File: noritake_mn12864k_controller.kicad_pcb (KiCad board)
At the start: 4 copper layers, 85 x 46.5 mm, 150 parts, among them J1 Conn_01x11, J2 USB_C_Receptacle_USB2.0, J3 TagConnect_TC2030_SWD, J4 Conn_01x18, Q1 AO3400A, Q10 2N7002, Q11 LBSS84LT1G, Q12 2N7002, Q13 TO-252, Q14 CJT04N15, Q15 2N7002, Q16 LBSS84LT1G, Q17 2N7002, Q18 S9015, Q2 AO3400A, Q3 S9015, Q4 AO3401A, Q5 AO3401A, Q6 S9015, Q7 2N7002, Q8 LBSS84LT1G, Q9 2N7002, T1 Wuerth 760390013, T2 Wuerth 760390013, T3 Wuerth 760390013, U1 SN74AVC8T245PW, U10 SRV05-4, U11 SRV05-4, U12 SRV05-4, U2 74HC14, U3 CD4051B, U4 MN12864K, U5 STM32F730R8T6, U6 NE555D, U7 74HC08, U8 SRV05-4, U9 XC6206PxxxMR

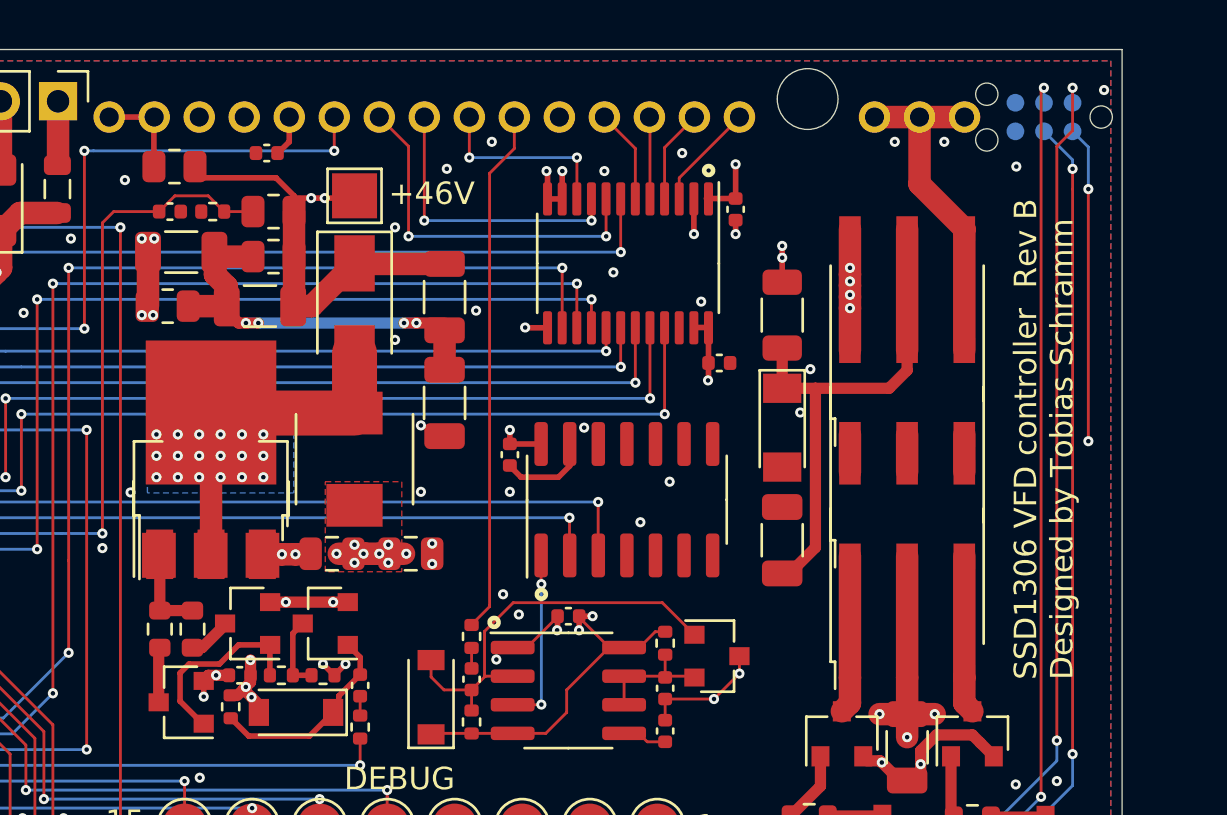
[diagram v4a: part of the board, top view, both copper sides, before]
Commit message: Add more VFD VDD2 bulk capacitance
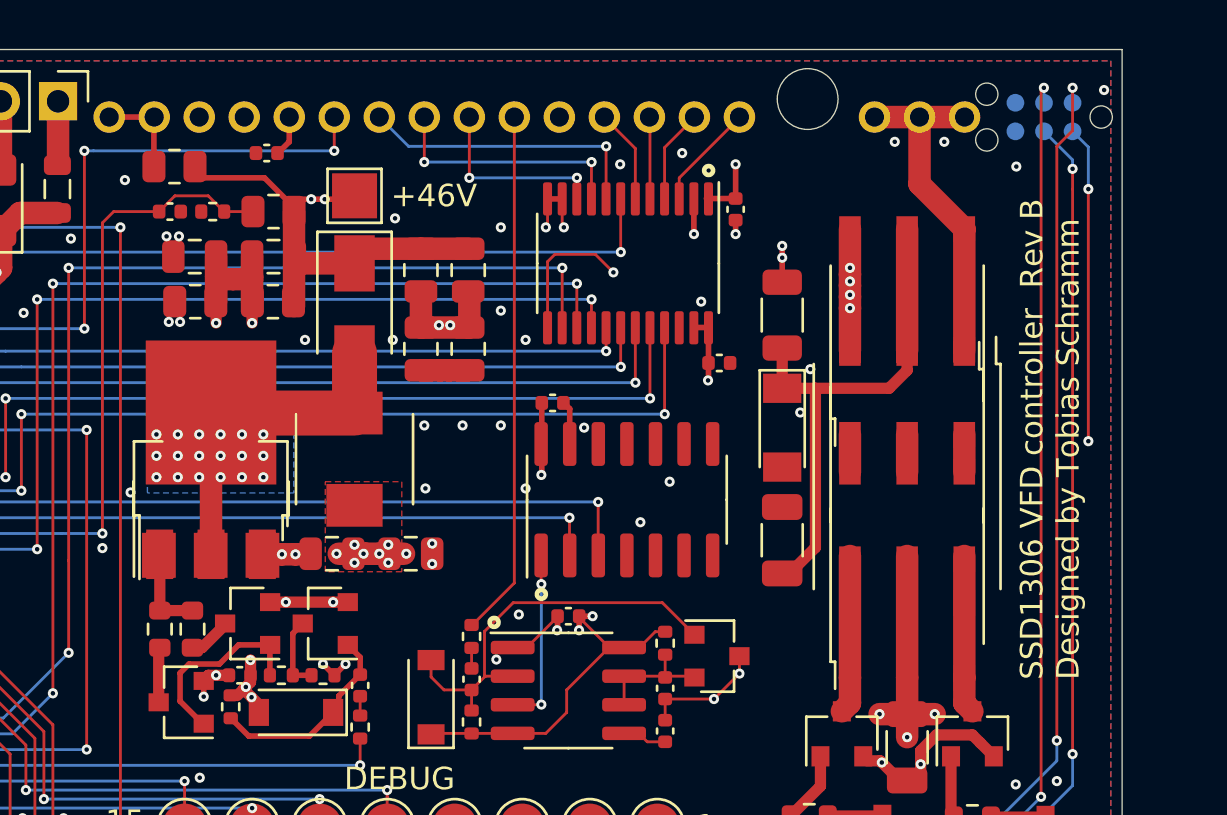
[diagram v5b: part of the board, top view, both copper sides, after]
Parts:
- added C40: 10uF, Capacitor_SMD:C_0805_2012Metric, F.Cu at (147.3, 104.7)
- added C41: 10uF, Capacitor_SMD:C_0805_2012Metric, F.Cu at (153.8, 108.8)
- added T4: Wuerth 760390013, Transformer_Würth:Transformer_Würth_12.60x8.30_6P, F.Cu at (175.4, 114.5)
- C30, C35, C38, C39: footprint Capacitor_SMD:C_1206_3216Metric -> Capacitor_SMD:C_0805_2012Metric
- moved C39 12.9 mm to (143.8, 104.7), turned to 180 degrees
- moved C35 12.8 mm to (155.9, 105.3), turned to 270 degrees
- moved C30 9.44 mm to (155.9, 108.8), turned to 270 degrees
- moved C27 2.98 mm to (159.7, 111.2), turned to 180 degrees
- moved R30 2.00 mm to (147.3, 106.7)
- moved C38 1.59 mm to (153.8, 105.3)
- moved R31 1.24 mm to (143.8, 106.7)
- turned T1 to 270 degrees
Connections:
- C30 pad 1: +48V -> Net-(C30-Pad1)
- C30 pad 2: Net-(C30-Pad2) -> GND
- C35 pad 1: Net-(C30-Pad2) -> +48V
- C35 pad 2: GND -> Net-(C30-Pad1)
- C38 pad 2: Net-(C30-Pad2) -> Net-(C30-Pad1)
- C39 pad 1: Net-(C30-Pad2) -> Net-(C30-Pad1)
- R30 pad 2: Net-(C30-Pad2) -> Net-(C30-Pad1)
- R31 pad 1: Net-(C30-Pad2) -> Net-(C30-Pad1)
- T1 pad 1: Net-(Q2-Pad3) -> Net-(T1-Pad1)
- T1 pad 2: +5V -> Net-(C8-Pad1)
- T1 pad 3: Net-(Q1-Pad3) -> Net-(T1-Pad3)
- T1 pad 4: Net-(T1-Pad4) -> Net-(Q2-Pad3)
- T1 pad 5: Net-(C8-Pad1) -> +5V
- T1 pad 6: Net-(T1-Pad6) -> Net-(Q1-Pad3)
- T3 pad 4: Net-(T1-Pad4) -> Net-(T1-Pad1)
- T3 pad 6: Net-(T1-Pad6) -> Net-(T1-Pad3)
- U4 pad 1: Net-(T1-Pad4) -> Net-(T1-Pad1)
- U4 pad 2: Net-(T1-Pad4) -> Net-(T1-Pad1)
- U4 pad 3: Net-(T1-Pad4) -> Net-(T1-Pad1)
- U4 pad 35: Net-(T1-Pad6) -> Net-(T1-Pad3)
- U4 pad 36: Net-(T1-Pad6) -> Net-(T1-Pad3)
- U4 pad 37: Net-(T1-Pad6) -> Net-(T1-Pad3)
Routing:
- net Net-(T1-Pad6): track 83.7 -> 0.00 mm, vias 4 -> 0
- net Net-(T1-Pad3): track 0.00 -> 83.7 mm, vias 0 -> 4
- net Net-(C30-Pad1): track 0.00 -> 23.5 mm, vias 0 -> 4
- net Net-(C30-Pad2): track 18.6 -> 0.00 mm, vias 4 -> 0
- net Net-(T1-Pad4): track 15.2 -> 0.00 mm
- net Net-(T1-Pad1): track 0.00 -> 15.2 mm
- net Net-(U1-Pad8): track 16.3 -> 13.0 mm, vias 2 -> 1
- net GND: track 88.8 -> 91.8 mm, vias 146 -> 147
- net Net-(U1-Pad9): track 13.0 -> 11.1 mm
- net +5V: track 76.3 -> 77.5 mm

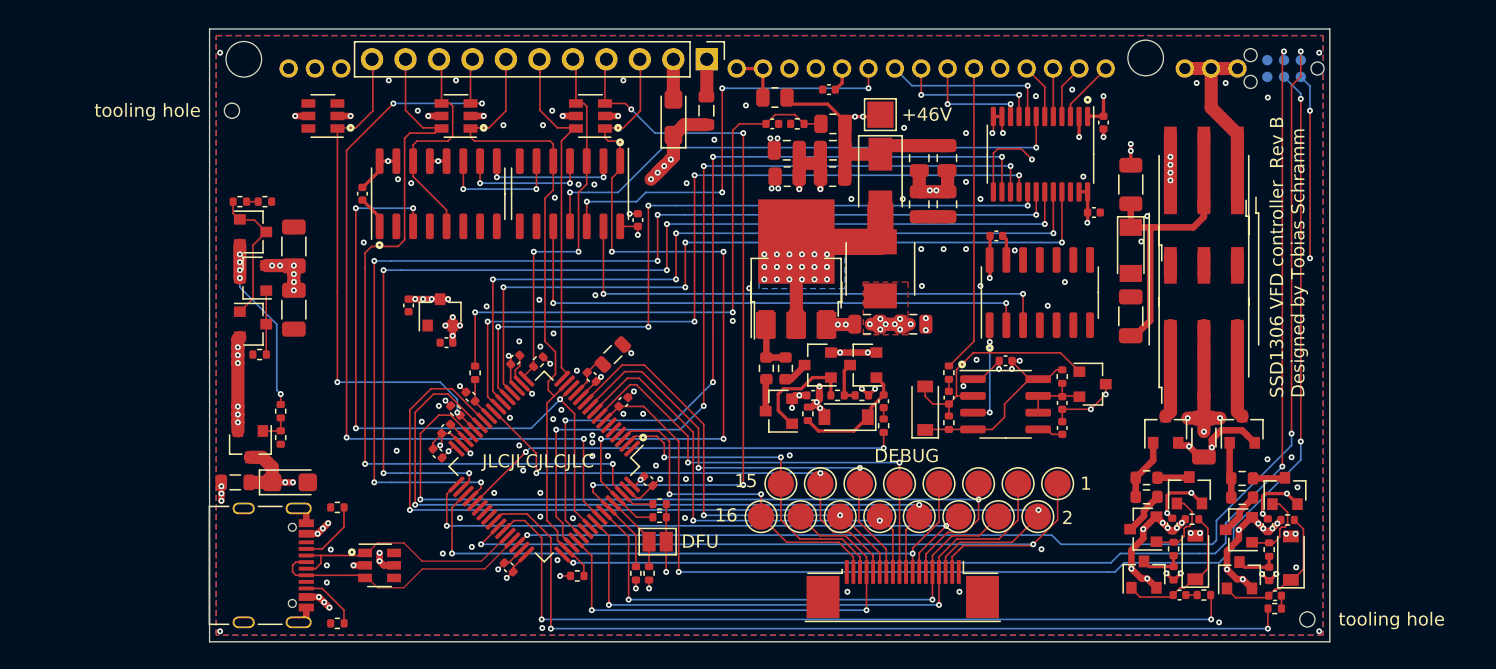
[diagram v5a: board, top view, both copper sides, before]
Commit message: Add optional mounting bracket
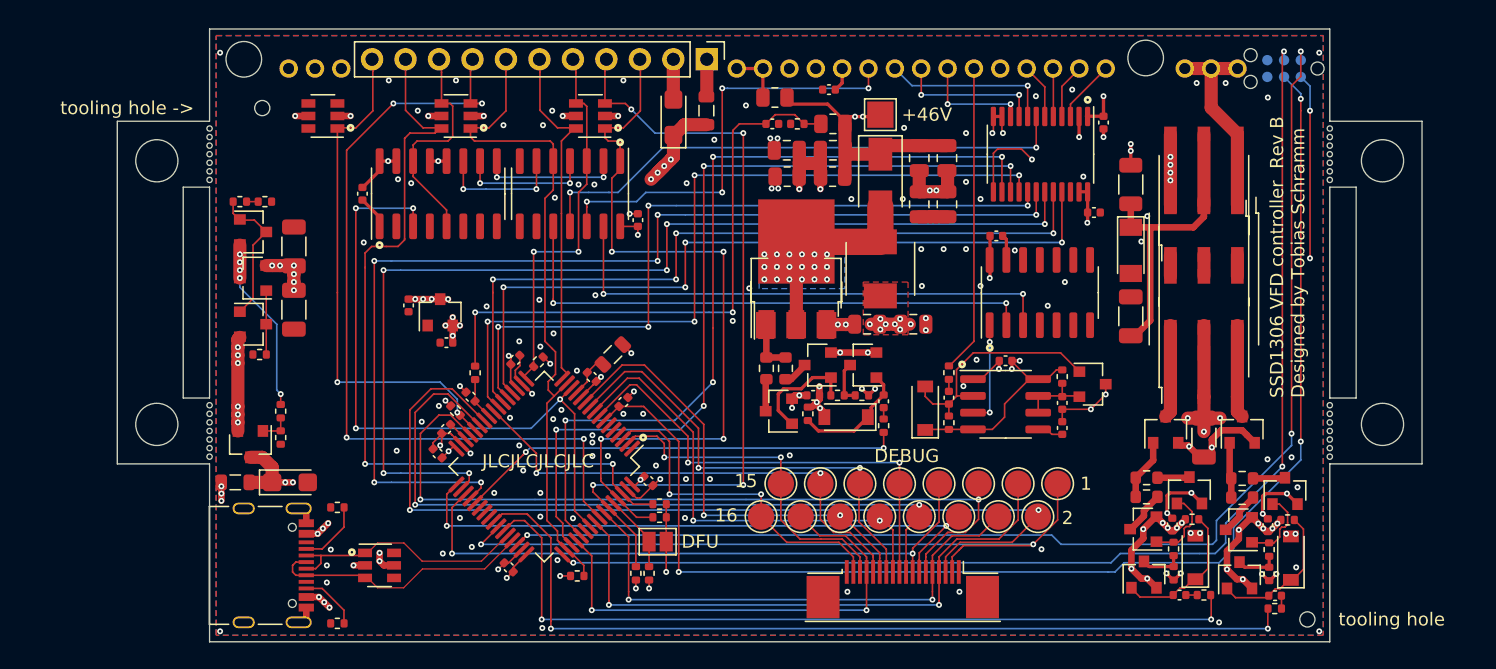
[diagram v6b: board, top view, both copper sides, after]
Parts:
- added H10: Perforation, Perforation:Perforation_0.4mm, F.Cu at (185.0, 128.0)
- added H11: Perforation, Perforation:Perforation_0.4mm, F.Cu at (185.0, 106.3)
- added H12: Perforation, Perforation:Perforation_0.4mm, F.Cu at (100.0, 107.0)
- added H13: Perforation, Perforation:Perforation_0.4mm, F.Cu at (185.0, 127.3)
- added H14: Perforation, Perforation:Perforation_0.4mm, F.Cu at (185.0, 105.7)
- added H15: Perforation, Perforation:Perforation_0.4mm, F.Cu at (100.0, 128.0)
- added H16: Perforation, Perforation:Perforation_0.4mm, F.Cu at (100.0, 106.3)
- added H17: Perforation, Perforation:Perforation_0.4mm, F.Cu at (185.0, 126.7)
- added H18: Perforation, Perforation:Perforation_0.4mm, F.Cu at (185.0, 105.0)
- added H19: Perforation, Perforation:Perforation_0.4mm, F.Cu at (100.0, 127.3)
- added H20: Perforation, Perforation:Perforation_0.4mm, F.Cu at (100.0, 105.7)
- added H21: Perforation, Perforation:Perforation_0.4mm, F.Cu at (185.0, 126.0)
- added H22: Perforation, Perforation:Perforation_0.4mm, F.Cu at (185.0, 104.3)
- added H23: Perforation, Perforation:Perforation_0.4mm, F.Cu at (100.0, 126.7)
- added H24: Perforation, Perforation:Perforation_0.4mm, F.Cu at (100.0, 105.0)
- added H25: Perforation, Perforation:Perforation_0.4mm, F.Cu at (185.0, 125.3)
- added H26: Perforation, Perforation:Perforation_0.4mm, F.Cu at (185.0, 103.7)
- added H27: Perforation, Perforation:Perforation_0.4mm, F.Cu at (100.0, 126.0)
- added H28: Perforation, Perforation:Perforation_0.4mm, F.Cu at (100.0, 104.3)
- added H29: Perforation, Perforation:Perforation_0.4mm, F.Cu at (185.0, 124.7)
- added H30: Perforation, Perforation:Perforation_0.4mm, F.Cu at (185.0, 103.0)
- added H31: Perforation, Perforation:Perforation_0.4mm, F.Cu at (100.0, 125.3)
- added H32: Perforation, Perforation:Perforation_0.4mm, F.Cu at (100.0, 103.7)
- added H33: Perforation, Perforation:Perforation_0.4mm, F.Cu at (185.0, 124.0)
- added H34: Perforation, Perforation:Perforation_0.4mm, F.Cu at (100.0, 124.7)
- added H35: Perforation, Perforation:Perforation_0.4mm, F.Cu at (100.0, 103.0)
- added H36: Perforation, Perforation:Perforation_0.4mm, F.Cu at (100.0, 124.0)
- added H5: MountingHole, MountingHole:MountingHole_3.2mm_M3, F.Cu at (189.0, 105.5)
- added H6: MountingHole, MountingHole:MountingHole_3.2mm_M3, F.Cu at (96.0, 125.5)
- added H7: MountingHole, MountingHole:MountingHole_3.2mm_M3, F.Cu at (96.0, 105.5)
- added H8: MountingHole, MountingHole:MountingHole_3.2mm_M3, F.Cu at (189.0, 125.5)
- added H9: Perforation, Perforation:Perforation_0.4mm, F.Cu at (185.0, 107.0)
- moved H1 2.31 mm to (104.0, 101.5)
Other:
- board size 85 x 46.5 mm -> 99 x 46.5 mm

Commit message: Less diseased power routing
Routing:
- net +48V: track 44.0 -> 41.7 mm
- net Net-(T1-Pad3): track 83.7 -> 82.5 mm
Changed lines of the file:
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@@
   (gr_line (start 185 123.5) (end 185 107.5) (layer Edge.Cuts) (width 0.05))
   (gr_line (start 100 142) (end 185 142) (layer Edge.Cuts) (width 0.05))
+  (via (at 155.95 103.6) (size 0.45) (drill 0.2) (layers F.Cu B.Cu) (net 21))
+  (segment (start 155.95 104.35) (end 155.95 103.6) (width 0.5) (layer F.Cu) (net 21))
   (segment (start 141.9875 100.7) (end 141.9875 98.5) (width 0.25) (layer F.Cu) (net 1))
   (segment (start 140 98.5) (end 142 98.5) (width 0.25) (layer F.Cu) (net 1))
@@
   (segment (start 108.55 134.95) (end 110.2 133.3) (width 0.127) (layer F.Cu) (net 19))
   (segment (start 110.2 133.3) (end 110.2 131.6) (width 0.127) (layer F.Cu) (net 19))
-  (segment (start 148.2125 102.7) (end 148.2125 106.9) (width 1) (layer F.Cu) (net 21))
-  (via (at 148.975 102.15) (size 0.45) (drill 0.2) (layers F.Cu B.Cu) (net 21))
+  (segment (start 148.2125 102.7) (end 148.2125 103.6875) (width 1) (layer F.Cu) (net 21))
   (segment (start 148.2125 102.15) (end 148.975 102.15) (width 0.25) (layer F.Cu) (net 21))
-  (via (at 149.575 102.15) (size 0.45) (drill 0.2) (layers F.Cu B.Cu) (net 21))
-  (segment (start 148.975 102.15) (end 149.575 102.15) (width 0.25) (layer Power) (net 21))
   (segment (start 149.575 102.15) (end 150.9 102.15) (width 0.25) (layer F.Cu) (net 21))
   (segment (start 148.975 102.15) (end 149.575 102.15) (width 0.25) (layer F.Cu) (net 21))
-  (via (at 169.9 104.225) (size 0.45) (drill 0.2) (layers F.Cu B.Cu) (net 21))
-  (via (at 169.9 104.75) (size 0.45) (drill 0.2) (layers F.Cu B.Cu) (net 21))
-  (segment (start 169.9 104.225) (end 169.9 104.75) (width 0.25) (layer Power) (net 21))
-  (segment (start 169.9 104.75) (end 169.9 105.85) (width 0.25) (layer F.Cu) (net 21))
-  (segment (start 169.9 104.225) (end 169.9 104.75) (width 0.25) (layer F.Cu) (net 21))
-  (segment (start 169.9 103.625) (end 169.9 104.225) (width 0.25) (layer Power) (net 21))
+  (via (at 169.9 107.175) (size 0.45) (drill 0.2) (layers F.Cu B.Cu) (net 21))
+  (via (at 169.9 106.65) (size 0.45) (drill 0.2) (layers F.Cu B.Cu) (net 21))
+  (segment (start 169.9 107.175) (end 169.9 106.65) (width 0.25) (layer Power) (net 21))
+  (segment (start 169.9 106.65) (end 169.9 105.55) (width 0.25) (layer F.Cu) (net 21))
+  (segment (start 169.9 107.175) (end 169.9 106.65) (width 0.25) (layer F.Cu) (net 21))
   (segment (start 150.9 105) (end 148.3 105) (width 1) (layer F.Cu) (net 21))
   (segment (start 155.95 104.35) (end 153.85 104.35) (width 1) (layer F.Cu) (net 21))
-  (segment (start 149.575 102.15) (end 168.425 102.15) (width 0.25) (layer Power) (net 21))
-  (segment (start 169.9 103.625) (end 168.425 102.15) (width 0.25) (layer Power) (net 21))
   (segment (start 148.2125 102.5125) (end 146.9 101.2) (width 0.25) (layer F.Cu) (net 21))
   (segment (start 148.2125 102.7) (end 148.2125 102.5125) (width 0.25) (layer F.Cu) (net 21))
   (segment (start 146.9 101.2) (end 143.8 101.2) (width 0.25) (layer F.Cu) (net 21))
   (segment (start 153.85 104.35) (end 150.9 104.35) (width 1) (layer F.Cu) (net 21))
+  (segment (start 148.2125 103.6875) (end 148.2125 106.9) (width 1) (layer F.Cu) (net 21))
+  (via (at 153.85 103.6) (size 0.45) (drill 0.2) (layers F.Cu B.Cu) (net 21))
+  (segment (start 153.85 104.35) (end 153.85 103.6) (width 0.5) (layer F.Cu) (net 21))
+  (segment (start 153.85 103.6) (end 155.95 103.6) (width 0.25) (layer Power) (net 21))
+  (segment (start 169.9 107.5) (end 169.9 107.175) (width 0.25) (layer Power) (net 21))
+  (segment (start 169.5 107.9) (end 169.9 107.5) (width 0.25) (layer Power) (net 21))
+  (segment (start 160.25 107.9) (end 169.5 107.9) (width 0.25) (layer Power) (net 21))
+  (segment (start 155.95 103.6) (end 160.25 107.9) (width 0.25) (layer Power) (net 21))
   (via (at 161.725 115.6) (size 0.45) (drill 0.2) (layers F.Cu B.Cu) (net 22))
   (via (at 129.89 115.6) (size 0.45) (drill 0.2) (layers F.Cu B.Cu) (net 22))
@@
   (segment (start 172.91 105.49) (end 172.91 103.475) (width 1) (layer F.Cu) (net 134))
   (via (at 172.91 105.2) (size 0.45) (drill 0.2) (layers F.Cu B.Cu) (net 134))
-  (segment (start 172.2 107.7) (end 172.91 106.99) (width 1) (layer Power) (net 134))
-  (segment (start 148.6 105.825) (end 155.125 105.825) (width 1) (layer Power) (net 134))
-  (segment (start 172.91 106.99) (end 172.91 105.49) (width 1) (layer Power) (net 134))
-  (segment (start 172.91 105.2) (end 172.91 105.49) (width 1) (layer Power) (net 134))
-  (segment (start 144.975 102.2) (end 148.6 105.825) (width 1) (layer Power) (net 134))
   (segment (start 131.375 103.825) (end 133 102.2) (width 1) (layer Power) (net 134))
-  (segment (start 133 102.2) (end 144.975 102.2) (width 1) (layer Power) (net 134))
   (segment (start 109.725 103.825) (end 131.375 103.825) (width 1) (layer Power) (net 134))
   (segment (start 108 102.1) (end 109.725 103.825) (width 1) (layer Power) (net 134))
   (segment (start 108 98.5) (end 108 102.1) (width 1) (layer Power) (net 134))
-  (segment (start 158.28 105.825) (end 160.155 107.7) (width 1) (layer Power) (net 134))
-  (segment (start 155.125 105.825) (end 158.28 105.825) (width 1) (layer Power) (net 134))
-  (segment (start 160.155 107.7) (end 172.2 107.7) (width 1) (layer Power) (net 134))
   (segment (start 177.99 108.867) (end 177.99 103.475) (width 1) (layer F.Cu) (net 133))
   (segment (start 176 98.5) (end 176 101.475) (width 1) (layer F.Cu) (net 133))
@@
   (segment (start 146.35 107.65) (end 154.55 107.65) (width 0.5) (layer Power) (net 132))
   (segment (start 155.15 107.75) (end 154.65 107.75) (width 0.5) (layer Power) (net 132))
+  (segment (start 170.213197 102.184999) (end 172.91 104.881802) (width 1) (layer Power) (net 134))
+  (segment (start 152.308799 102.184999) (end 170.213197 102.184999) (width 1) (layer Power) (net 134))
+  (segment (start 152.293798 102.2) (end 152.308799 102.184999) (width 1) (layer Power) (net 134))
+  (segment (start 133 102.2) (end 152.293798 102.2) (width 1) (layer Power) (net 134))
+  (segment (start 172.91 104.881802) (end 172.91 106.99) (width 1) (layer Power) (net 134))
   (zone (net 0) (net_name "") (layer F.Cu) (hatch edge 0.508)
     (connect_pads (clearance 0.508))
